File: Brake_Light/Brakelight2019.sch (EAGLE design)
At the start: 49 parts

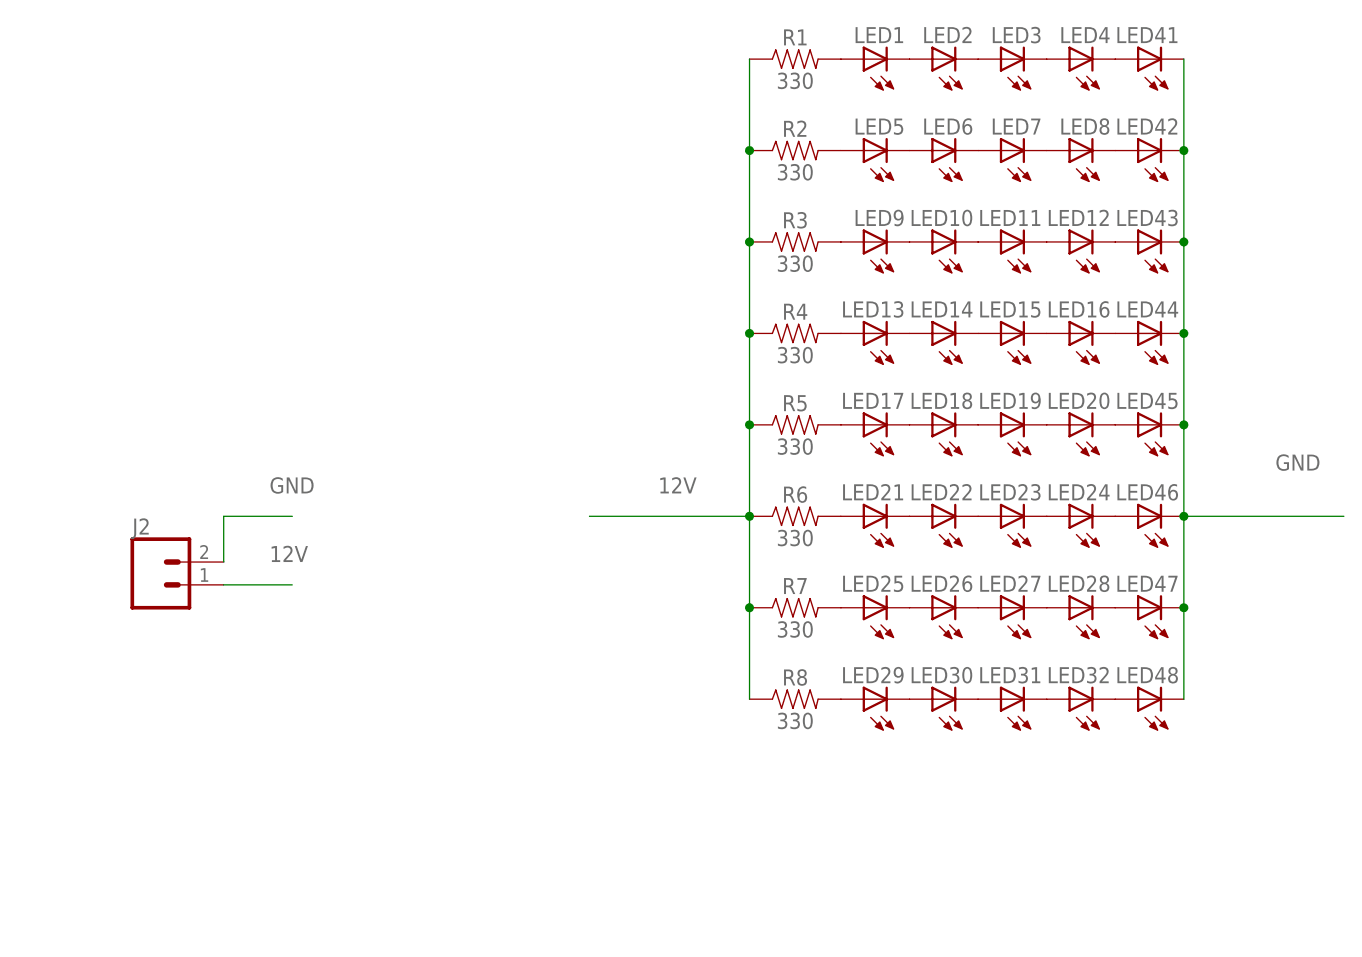
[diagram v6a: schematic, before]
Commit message: Add files via upload
Changed resistor values
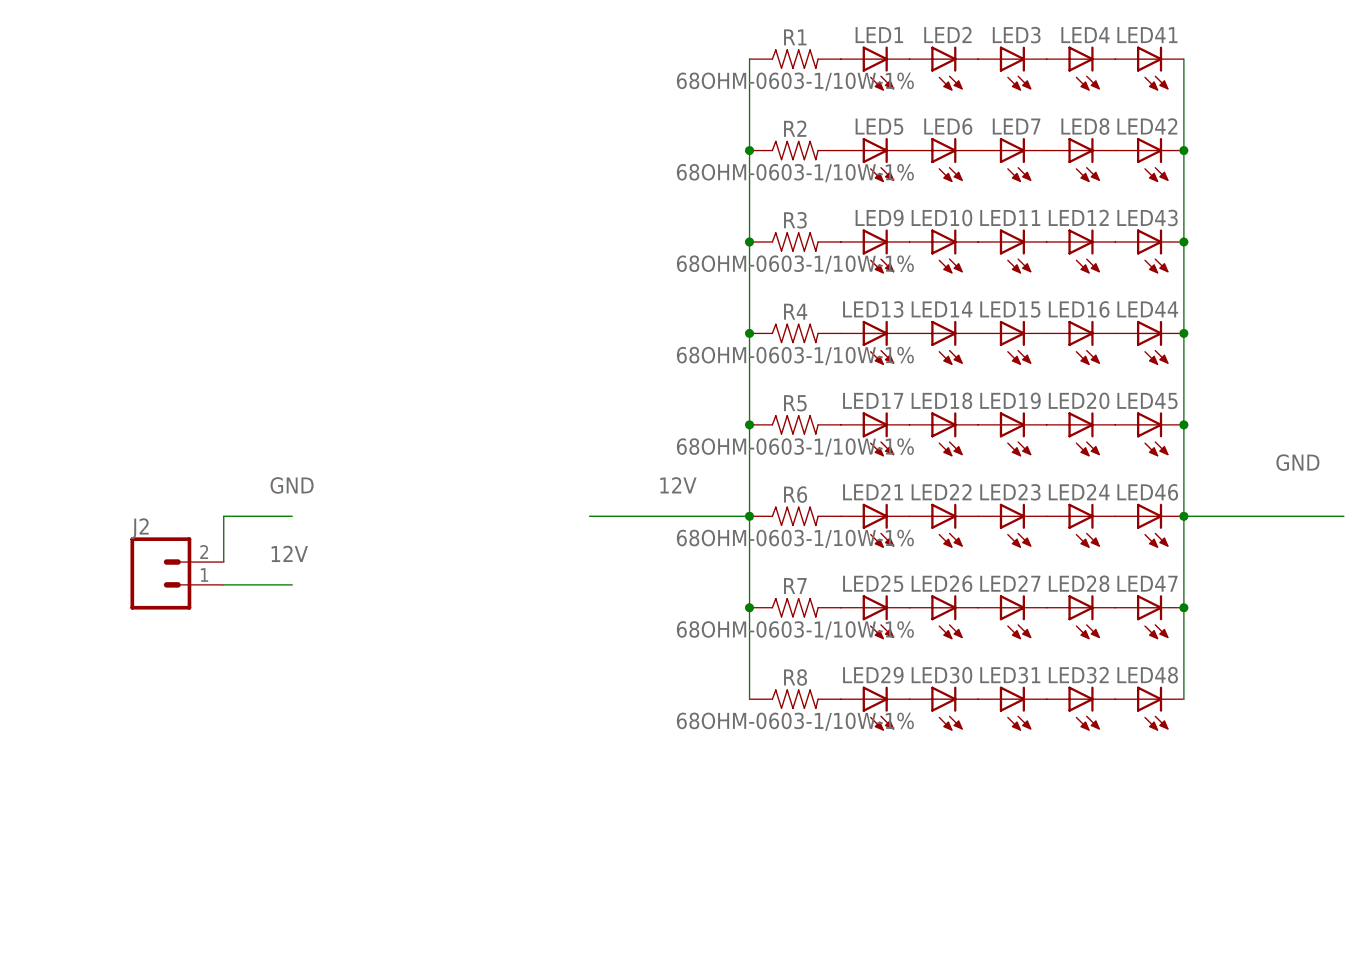
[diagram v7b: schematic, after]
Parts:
- R1, R2, R3, R4, R5, R6, R7, R8: value 330 -> 68OHM-0603-1/10W-1%; device SparkFun-Resistors:330OHM-0603-1/10W-1% -> SparkFun-Resistors:68OHM-0603-1/10W-1%
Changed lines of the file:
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@@
 <?xml version="1.0" encoding="utf-8"?>
 <!DOCTYPE eagle SYSTEM "eagle.dtd">
-<eagle version="9.1.0">
+<eagle version="9.1.3">
 <drawing>
 <settings>
@@
 </classes>
 <parts>
-<part name="R1" library="SparkFun-Resistors" library_urn="urn:adsk.eagle:library:532" deviceset="330OHM" device="-0603-1/10W-1%" package3d_urn="urn:adsk.eagle:package:39650/1" value="330"/>
-<part name="R2" library="SparkFun-Resistors" library_urn="urn:adsk.eagle:library:532" deviceset="330OHM" device="-0603-1/10W-1%" package3d_urn="urn:adsk.eagle:package:39650/1" value="330"/>
-<part name="R3" library="SparkFun-Resistors" library_urn="urn:adsk.eagle:library:532" deviceset="330OHM" device="-0603-1/10W-1%" package3d_urn="urn:adsk.eagle:package:39650/1" value="330"/>
-<part name="R4" library="SparkFun-Resistors" library_urn="urn:adsk.eagle:library:532" deviceset="330OHM" device="-0603-1/10W-1%" package3d_urn="urn:adsk.eagle:package:39650/1" value="330"/>
-<part name="R5" library="SparkFun-Resistors" library_urn="urn:adsk.eagle:library:532" deviceset="330OHM" device="-0603-1/10W-1%" package3d_urn="urn:adsk.eagle:package:39650/1" value="330"/>
-<part name="R6" library="SparkFun-Resistors" library_urn="urn:adsk.eagle:library:532" deviceset="330OHM" device="-0603-1/10W-1%" package3d_urn="urn:adsk.eagle:package:39650/1" value="330"/>
-<part name="R7" library="SparkFun-Resistors" library_urn="urn:adsk.eagle:library:532" deviceset="330OHM" device="-0603-1/10W-1%" package3d_urn="urn:adsk.eagle:package:39650/1" value="330"/>
-<part name="R8" library="SparkFun-Resistors" library_urn="urn:adsk.eagle:library:532" deviceset="330OHM" device="-0603-1/10W-1%" package3d_urn="urn:adsk.eagle:package:39650/1" value="330"/>
 <part name="LED1" library="adafruit" library_urn="urn:adsk.eagle:library:420" deviceset="LED" device="5MM" package3d_urn="urn:adsk.eagle:package:6240538/1"/>
 <part name="LED2" library="adafruit" library_urn="urn:adsk.eagle:library:420" deviceset="LED" device="5MM" package3d_urn="urn:adsk.eagle:package:6240538/1"/>
@@
 <part name="LED48" library="adafruit" library_urn="urn:adsk.eagle:library:420" deviceset="LED" device="5MM" package3d_urn="urn:adsk.eagle:package:6240538/1"/>
 <part name="J2" library="SparkFun-Connectors" library_urn="urn:adsk.eagle:library:513" deviceset="CONN_02" device="POLAR" package3d_urn="urn:adsk.eagle:package:38040/1"/>
+<part name="R1" library="SparkFun-Resistors" library_urn="urn:adsk.eagle:library:532" deviceset="68OHM" device="-0603-1/10W-1%" package3d_urn="urn:adsk.eagle:package:39650/1"/>
+<part name="R2" library="SparkFun-Resistors" library_urn="urn:adsk.eagle:library:532" deviceset="68OHM" device="-0603-1/10W-1%" package3d_urn="urn:adsk.eagle:package:39650/1"/>
+<part name="R3" library="SparkFun-Resistors" library_urn="urn:adsk.eagle:library:532" deviceset="68OHM" device="-0603-1/10W-1%" package3d_urn="urn:adsk.eagle:package:39650/1"/>
+<part name="R4" library="SparkFun-Resistors" library_urn="urn:adsk.eagle:library:532" deviceset="68OHM" device="-0603-1/10W-1%" package3d_urn="urn:adsk.eagle:package:39650/1"/>
+<part name="R5" library="SparkFun-Resistors" library_urn="urn:adsk.eagle:library:532" deviceset="68OHM" device="-0603-1/10W-1%" package3d_urn="urn:adsk.eagle:package:39650/1"/>
+<part name="R6" library="SparkFun-Resistors" library_urn="urn:adsk.eagle:library:532" deviceset="68OHM" device="-0603-1/10W-1%" package3d_urn="urn:adsk.eagle:package:39650/1"/>
+<part name="R7" library="SparkFun-Resistors" library_urn="urn:adsk.eagle:library:532" deviceset="68OHM" device="-0603-1/10W-1%" package3d_urn="urn:adsk.eagle:package:39650/1"/>
+<part name="R8" library="SparkFun-Resistors" library_urn="urn:adsk.eagle:library:532" deviceset="68OHM" device="-0603-1/10W-1%" package3d_urn="urn:adsk.eagle:package:39650/1"/>
 </parts>
 <sheets>
@@
 </plain>
 <instances>
-<instance part="R1" gate="G$1" x="93.98" y="132.08"/>
-<instance part="R2" gate="G$1" x="93.98" y="121.92"/>
-<instance part="R3" gate="G$1" x="93.98" y="111.76"/>
-<instance part="R4" gate="G$1" x="93.98" y="101.6"/>
-<instance part="R5" gate="G$1" x="93.98" y="91.44"/>
-<instance part="R6" gate="G$1" x="93.98" y="81.28"/>
-<instance part="R7" gate="G$1" x="93.98" y="71.12"/>
-<instance part="R8" gate="G$1" x="93.98" y="60.96"/>
 <instance part="LED1" gate="G$1" x="101.6" y="132.08" rot="R90"/>
 <instance part="LED2" gate="G$1" x="109.22" y="132.08" rot="R90"/>
@@
 <instance part="LED48" gate="G$1" x="132.08" y="60.96" rot="R90"/>
 <instance part="J2" gate="G$1" x="22.86" y="73.66"/>
+<instance part="R1" gate="G$1" x="93.98" y="132.08"/>
+<instance part="R2" gate="G$1" x="93.98" y="121.92"/>
+<instance part="R3" gate="G$1" x="93.98" y="111.76"/>
+<instance part="R4" gate="G$1" x="93.98" y="101.6"/>
+<instance part="R5" gate="G$1" x="93.98" y="91.44"/>
+<instance part="R6" gate="G$1" x="93.98" y="81.28"/>
+<instance part="R7" gate="G$1" x="93.98" y="71.12"/>
+<instance part="R8" gate="G$1" x="93.98" y="60.96"/>
 </instances>
 <busses>
@@
 <net name="12V" class="0">
 <segment>
+<wire x1="88.9" y1="132.08" x2="88.9" y2="121.92" width="0.1524" layer="91"/>
+<junction x="88.9" y="81.28"/>
+<wire x1="88.9" y1="121.92" x2="88.9" y2="111.76" width="0.1524" layer="91"/>
+<wire x1="88.9" y1="111.76" x2="88.9" y2="101.6" width="0.1524" layer="91"/>
+<wire x1="88.9" y1="101.6" x2="88.9" y2="91.44" width="0.1524" layer="91"/>
+<wire x1="88.9" y1="91.44" x2="88.9" y2="81.28" width="0.1524" layer="91"/>
+<wire x1="88.9" y1="81.28" x2="88.9" y2="71.12" width="0.1524" layer="91"/>
+<wire x1="88.9" y1="71.12" x2="88.9" y2="60.96" width="0.1524" layer="91"/>
+<wire x1="88.9" y1="81.28" x2="71.12" y2="81.28" width="0.1524" layer="91"/>
+<label x="78.74" y="83.82" size="1.778" layer="95"/>
 <pinref part="R1" gate="G$1" pin="1"/>
 <pinref part="R2" gate="G$1" pin="1"/>
-<wire x1="88.9" y1="132.08" x2="88.9" y2="121.92" width="0.1524" layer="91"/>
+<junction x="88.9" y="121.92"/>
 <pinref part="R3" gate="G$1" pin="1"/>
-<wire x1="88.9" y1="121.92" x2="88.9" y2="111.76" width="0.1524" layer="91"/>
-<junction x="88.9" y="121.92"/>
+<junction x="88.9" y="111.76"/>
 <pinref part="R4" gate="G$1" pin="1"/>
-<wire x1="88.9" y1="111.76" x2="88.9" y2="101.6" width="0.1524" layer="91"/>
-<junction x="88.9" y="111.76"/>
+<junction x="88.9" y="101.6"/>
 <pinref part="R5" gate="G$1" pin="1"/>
-<wire x1="88.9" y1="101.6" x2="88.9" y2="91.44" width="0.1524" layer="91"/>
-<junction x="88.9" y="101.6"/>
+<junction x="88.9" y="91.44"/>
 <pinref part="R6" gate="G$1" pin="1"/>
-<wire x1="88.9" y1="91.44" x2="88.9" y2="81.28" width="0.1524" layer="91"/>
-<junction x="88.9" y="91.44"/>
 <pinref part="R7" gate="G$1" pin="1"/>
-<wire x1="88.9" y1="81.28" x2="88.9" y2="71.12" width="0.1524" layer="91"/>
-<junction x="88.9" y="81.28"/>
+<junction x="88.9" y="71.12"/>
 <pinref part="R8" gate="G$1" pin="1"/>
-<wire x1="88.9" y1="71.12" x2="88.9" y2="60.96" width="0.1524" layer="91"/>
-<junction x="88.9" y="71.12"/>
-<wire x1="88.9" y1="81.28" x2="71.12" y2="81.28" width="0.1524" layer="91"/>
-<label x="78.74" y="83.82" size="1.778" layer="95"/>
 </segment>
 <segment>
@@
 </segment>
 </net>
-<net name="N$1" class="0">
-<segment>
-<pinref part="R1" gate="G$1" pin="2"/>
-<pinref part="LED1" gate="G$1" pin="A"/>
-</segment>
-</net>
 <net name="N$2" class="0">
 <segment>
@@
 </segment>
 </net>
-<net name="N$5" class="0">
-<segment>
-<pinref part="R2" gate="G$1" pin="2"/>
-<pinref part="LED5" gate="G$1" pin="A"/>
-</segment>
-</net>
 <net name="N$6" class="0">
 <segment>
@@
 </segment>
 </net>
-<net name="N$9" class="0">
-<segment>
-<pinref part="R3" gate="G$1" pin="2"/>
-<pinref part="LED9" gate="G$1" pin="A"/>
-</segment>
-</net>
 <net name="N$10" class="0">
 <segment>
@@
 </segment>
 </net>
-<net name="N$13" class="0">
-<segment>
-<pinref part="R4" gate="G$1" pin="2"/>
-<pinref part="LED13" gate="G$1" pin="A"/>
-</segment>
-</net>
 <net name="N$14" class="0">
 <segment>
@@
 </segment>
 </net>
-<net name="N$17" class="0">
-<segment>
-<pinref part="R5" gate="G$1" pin="2"/>
-<pinref part="LED17" gate="G$1" pin="A"/>
-</segment>
-</net>
 <net name="N$18" class="0">
 <segment>
@@
 </segment>
 </net>
-<net name="N$21" class="0">
-<segment>
-<pinref part="R6" gate="G$1" pin="2"/>
-<pinref part="LED21" gate="G$1" pin="A"/>
-</segment>
-</net>
 <net name="N$22" class="0">
 <segment>
@@
 </segment>
 </net>
-<net name="N$25" class="0">
-<segment>
-<pinref part="R7" gate="G$1" pin="2"/>
-<pinref part="LED25" gate="G$1" pin="A"/>
-</segment>
-</net>
 <net name="N$26" class="0">
 <segment>
@@
 </segment>
 </net>
-<net name="N$29" class="0">
-<segment>
-<pinref part="R8" gate="G$1" pin="2"/>
-<pinref part="LED29" gate="G$1" pin="A"/>
-</segment>
-</net>
 <net name="N$30" class="0">
 <segment>
@@
 </segment>
 </net>
+<net name="N$1" class="0">
+<segment>
+<pinref part="LED1" gate="G$1" pin="A"/>
+<pinref part="R1" gate="G$1" pin="2"/>
+</segment>
+</net>
+<net name="N$5" class="0">
+<segment>
+<pinref part="LED5" gate="G$1" pin="A"/>
+<pinref part="R2" gate="G$1" pin="2"/>
+</segment>
+</net>
+<net name="N$9" class="0">
+<segment>
+<pinref part="LED9" gate="G$1" pin="A"/>
+<pinref part="R3" gate="G$1" pin="2"/>
+</segment>
+</net>
+<net name="N$13" class="0">
+<segment>
+<pinref part="LED13" gate="G$1" pin="A"/>
+<pinref part="R4" gate="G$1" pin="2"/>
+</segment>
+</net>
+<net name="N$17" class="0">
+<segment>
+<pinref part="LED17" gate="G$1" pin="A"/>
+<pinref part="R5" gate="G$1" pin="2"/>
+</segment>
+</net>
+<net name="N$21" class="0">
+<segment>
+<pinref part="LED21" gate="G$1" pin="A"/>
+<pinref part="R6" gate="G$1" pin="2"/>
+</segment>
+</net>
+<net name="N$25" class="0">
+<segment>
+<pinref part="LED25" gate="G$1" pin="A"/>
+<pinref part="R7" gate="G$1" pin="2"/>
+</segment>
+</net>
+<net name="N$29" class="0">
+<segment>
+<pinref part="LED29" gate="G$1" pin="A"/>
+<pinref part="R8" gate="G$1" pin="2"/>
+</segment>
+</net>

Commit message: Add files via upload
Brakelight is done!
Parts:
- removed LED41, LED42, LED43, LED44, LED45, LED46, LED47, LED48: (no value), adafruit:LED5MM
- added LED33, LED34, LED35, LED36, LED37, LED38, LED39, LED40: (no value), adafruit:LED5MM
- added R10, R9: 68OHM-0603-1/10W-1%, SparkFun-Resistors:68OHM-0603-1/10W-1%
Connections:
- removed net N$41: LED4.C, LED41.A
- removed net N$42: LED42.A, LED8.C
- removed net N$43: LED12.C, LED43.A
- removed net N$44: LED16.C, LED44.A
- removed net N$45: LED20.C, LED45.A
- removed net N$46: LED24.C, LED46.A
- removed net N$47: LED28.C, LED47.A
- removed net N$48: LED32.C, LED48.A
- new net N$33: LED33.A, R9.2
- new net N$34: LED33.C, LED34.A
- new net N$35: LED34.C, LED35.A
- new net N$36: LED35.C, LED36.A
- new net N$37: LED37.A, R10.2
- new net N$38: LED37.C, LED38.A
- new net N$39: LED38.C, LED39.A
- new net N$40: LED39.C, LED40.A
- net 12V: now also R10.1, R9.1
- net GND: now also LED12.C, LED16.C, LED20.C, LED24.C, LED28.C, LED32.C, LED36.C, LED4.C, LED40.C, LED8.C; no longer LED41.C, LED42.C, LED43.C, LED44.C, LED45.C, LED46.C, LED47.C, LED48.C
